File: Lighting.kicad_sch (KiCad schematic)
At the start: 5 parts, among them U4 TXS0101DBV

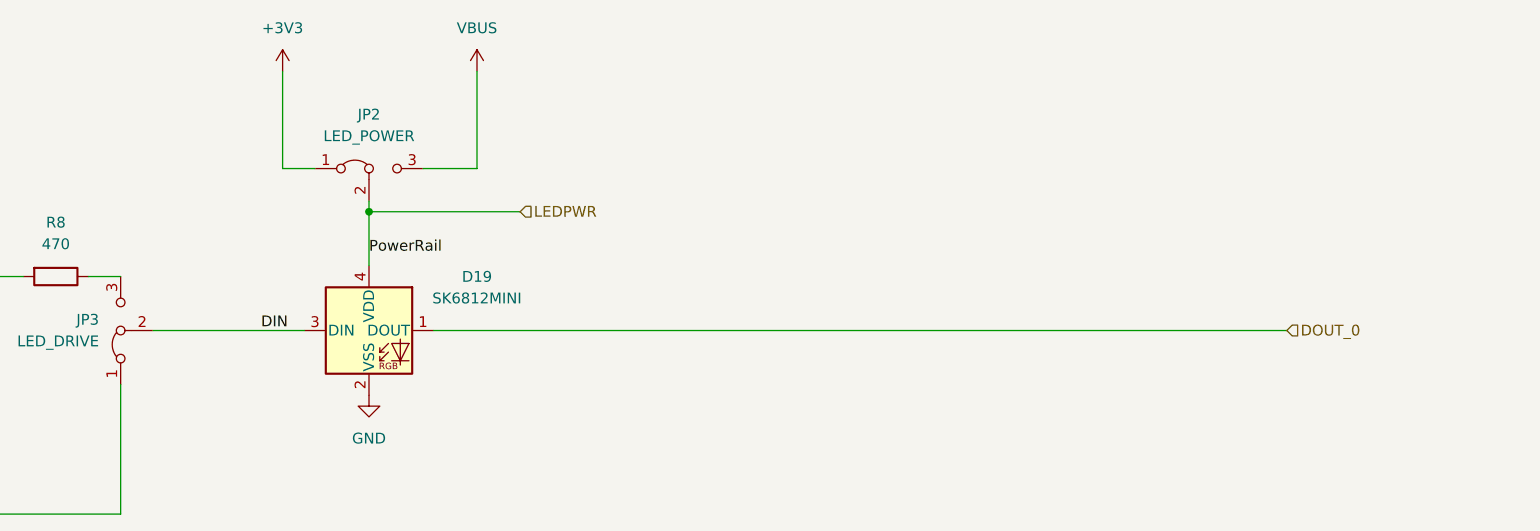
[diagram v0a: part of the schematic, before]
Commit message: WIP: Updated SK6812Mini to SK6812Mini-E and remapped ref des keys between PCB and Schematic.
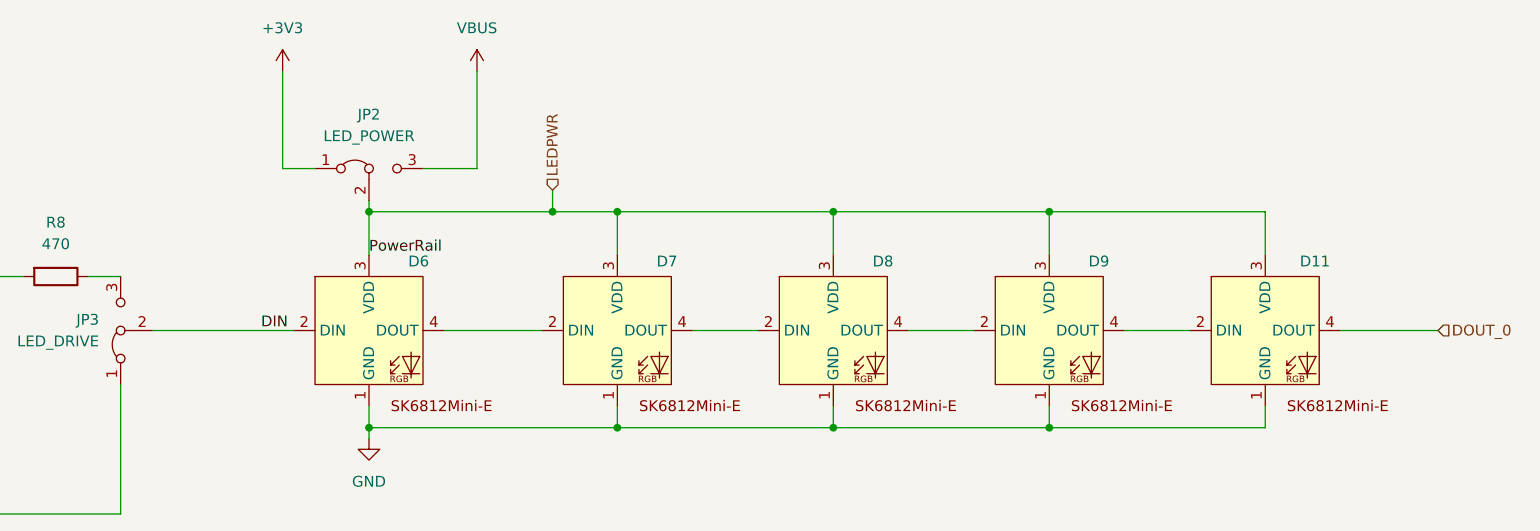
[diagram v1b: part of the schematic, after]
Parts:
- removed D19: SK6812MINI, LED_SMD:LED_SK6812MINI_PLCC4_3.5x3.5mm_P1.75mm, symbol LED:SK6812MINI
- added D11, D6, D7, D8, D9: ~, Extra:SK6812-MINI-E_ReverseMount, symbol Extra:SK6812Mini-E
- JP2, JP3: footprint (none) -> Connector_PinSocket_2.54mm:PinSocket_1x03_P2.54mm_Vertical
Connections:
- net DIN: now also D6.2 (DIN)
- net DOUT_0: now also D11.4 (DOUT)
- net GND: now also D11.1 (GND), D6.1 (GND), D7.1 (GND), D8.1 (GND), D9.1 (GND)
- net LEDPWR: now also D11.3 (VDD), D6.3 (VDD), D7.3 (VDD), D8.3 (VDD), D9.3 (VDD)
- new net: D8.4 (DOUT), D9.2 (DIN)
- new net: D11.2 (DIN), D9.4 (DOUT)
- new net: D6.4 (DOUT), D7.2 (DIN)
- new net: D7.4 (DOUT), D8.2 (DIN)

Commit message: Placing nearly all components onto the PCB. Removing the 9Vto5V battery input stage from populating onto the PCB.
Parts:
- R8: footprint Resistor_SMD:R_0603_1608Metric_Pad0.98x0.95mm_HandSolder -> Resistor_SMD:R_0805_2012Metric_Pad1.20x1.40mm_HandSolder
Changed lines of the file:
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@@
 			)
 		)
-		(property "Footprint" "Resistor_SMD:R_0603_1608Metric_Pad0.98x0.95mm_HandSolder"
+		(property "Footprint" "Resistor_SMD:R_0805_2012Metric_Pad1.20x1.40mm_HandSolder"
 			(at 88.9 47.752 90)
 			(effects

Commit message: Added testpoints, finished placing components, fixed footprint mapping, and ready to start routing tracks.
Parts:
- removed D11: ~, Extra:SK6812-MINI-E_ReverseMount, symbol Extra:SK6812Mini-E
- JP2, JP3: footprint Connector_PinSocket_2.54mm:PinSocket_1x03_P2.54mm_Vertical -> Connector_PinHeader_2.54mm:PinHeader_1x03_P2.54mm_Vertical
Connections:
- net DOUT_0: now also D9.4 (DOUT)
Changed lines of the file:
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@@
-	)
-	(junction
-		(at 205.74 67.31)
-		(diameter 0)
-		(color 0 0 0 0)
 	)
 	(junction
@@
 	)
 	(junction
-		(at 205.74 41.91)
-		(diameter 0)
-		(color 0 0 0 0)
-	)
-	(junction
 		(at 154.94 41.91)
 		(diameter 0)
@@
 	(wire
 		(pts
-			(xy 205.74 41.91) (xy 231.14 41.91)
-		)
-		(stroke
-			(width 0)
-			(type default)
-		)
-	)
-	(wire
-		(pts
 			(xy 132.08 36.83) (xy 138.43 36.83)
 		)
@@
 	(wire
 		(pts
-			(xy 240.03 55.88) (xy 251.46 55.88)
-		)
-		(stroke
-			(width 0)
-			(type default)
-		)
-	)
-	(wire
-		(pts
 			(xy 180.34 46.99) (xy 180.34 41.91)
 		)
@@
 	(wire
 		(pts
-			(xy 231.14 64.77) (xy 231.14 67.31)
-		)
-		(stroke
-			(width 0)
-			(type default)
-		)
-	)
-	(wire
-		(pts
 			(xy 205.74 46.99) (xy 205.74 41.91)
 		)
@@
 	(wire
 		(pts
-			(xy 231.14 46.99) (xy 231.14 41.91)
-		)
-		(stroke
-			(width 0)
-			(type default)
-		)
-	)
-	(wire
-		(pts
 			(xy 154.94 46.99) (xy 154.94 41.91)
 		)
@@
 		(pts
 			(xy 180.34 41.91) (xy 205.74 41.91)
-		)
-		(stroke
-			(width 0)
-			(type default)
-		)
-	)
-	(wire
-		(pts
-			(xy 205.74 67.31) (xy 231.14 67.31)
 		)
 		(stroke
@@
 	(hierarchical_label "DOUT_0"
 		(shape input)
-		(at 251.46 55.88 0)
+		(at 222.25 55.88 0)
 		(fields_autoplaced yes)
 		(effects
@@
 			)
 		)
-		(property "Footprint" "Connector_PinSocket_2.54mm:PinSocket_1x03_P2.54mm_Vertical"
+		(property "Footprint" "Connector_PinHeader_2.54mm:PinHeader_1x03_P2.54mm_Vertical"
 			(at 125.73 36.83 0)
 			(effects
@@
 	)
 	(symbol
-		(lib_id "Extra:SK6812Mini-E")
-		(at 231.14 55.88 0)
-		(unit 1)
-		(exclude_from_sim no)
-		(in_bom yes)
-		(on_board yes)
-		(dnp no)
-		(property "Reference" "D11"
-			(at 236.982 47.752 0)
-			(effects
-				(font
-					(size 1.27 1.27)
-				)
-			)
-		)
-		(property "Value" "~"
-			(at 250.19 52.7365 0)
-			(effects
-				(font
-					(size 1.27 1.27)
-				)
-			)
-		)
-		(property "Footprint" "Extra:SK6812-MINI-E_ReverseMount"
-			(at 231.14 55.88 0)
-			(effects
-				(font
-					(size 1.27 1.27)
-				)
-				(hide yes)
-			)
-		)
-		(property "Datasheet" ""
-			(at 231.14 55.88 0)
-			(effects
-				(font
-					(size 1.27 1.27)
-				)
-				(hide yes)
-			)
-		)
-		(property "Description" ""
-			(at 231.14 55.88 0)
-			(effects
-				(font
-					(size 1.27 1.27)
-				)
-				(hide yes)
-			)
-		)
-		(pin "3"
-		)
-		(pin "4"
-		)
-		(pin "1"
-		)
-		(pin "2"
-		)
-		(instances
-			(project "WeddingCenterPieces"
-				(path "/4e0ee48d-0121-4621-a533-4795bdfb88f1/959cab23-3f14-4c5e-8fa4-11c71d6f64e0"
-					(reference "D11")
-					(unit 1)
-				)
-			)
-		)
-	)
-	(symbol
 		(lib_id "power:VBUS")
 		(at 138.43 25.4 0)
@@
 			)
 		)
-		(property "Footprint" "Connector_PinSocket_2.54mm:PinSocket_1x03_P2.54mm_Vertical"
+		(property "Footprint" "Connector_PinHeader_2.54mm:PinHeader_1x03_P2.54mm_Vertical"
 			(at 96.52 55.88 0)
 			(effects

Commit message: Updating SK6812 circuit to match suggested application from datasheet, adding a resistor at the last DOut and filter caps to each LED.
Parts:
- added C19, C2, C20, C21: 100nF, Capacitor_SMD:C_0805_2012Metric_Pad1.18x1.45mm_HandSolder, symbol Device:C
- added R15: 470, Resistor_SMD:R_0805_2012Metric_Pad1.20x1.40mm_HandSolder, symbol Device:R
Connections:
- net DIN: now also R8.1; no longer JP3.2 (C)
- net DOUT_0: now also R15.1; no longer D9.4 (DOUT)
- net GND: now also C19.2, C2.2, C20.2, C21.2
- net LEDPWR: now also C19.1, C2.1, C20.1, C21.1
- net at JP3.3 (B): now also U4.4 (B); no longer R8.1
- net at R8.2: now also JP3.2 (C); no longer U4.4 (B)
- new net: D9.4 (DOUT), R15.2
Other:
- moved on the sheet: JP3, R8

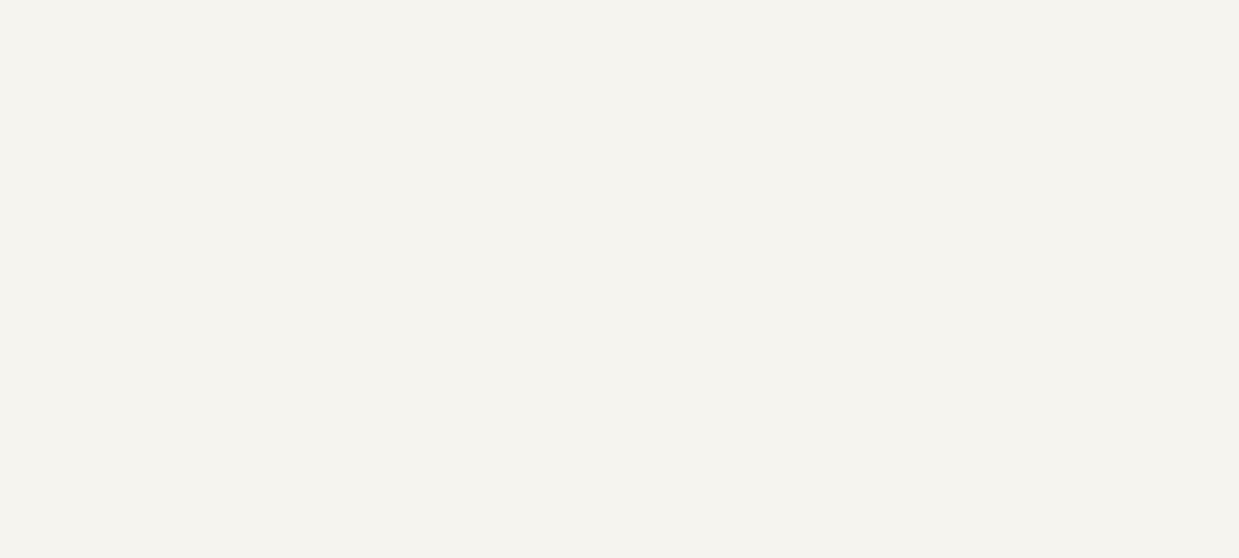
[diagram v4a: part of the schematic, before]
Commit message: Adding additional LEDs and driver to test per-key LEDs, updating net classes and design constraints, and starting to route tracks.
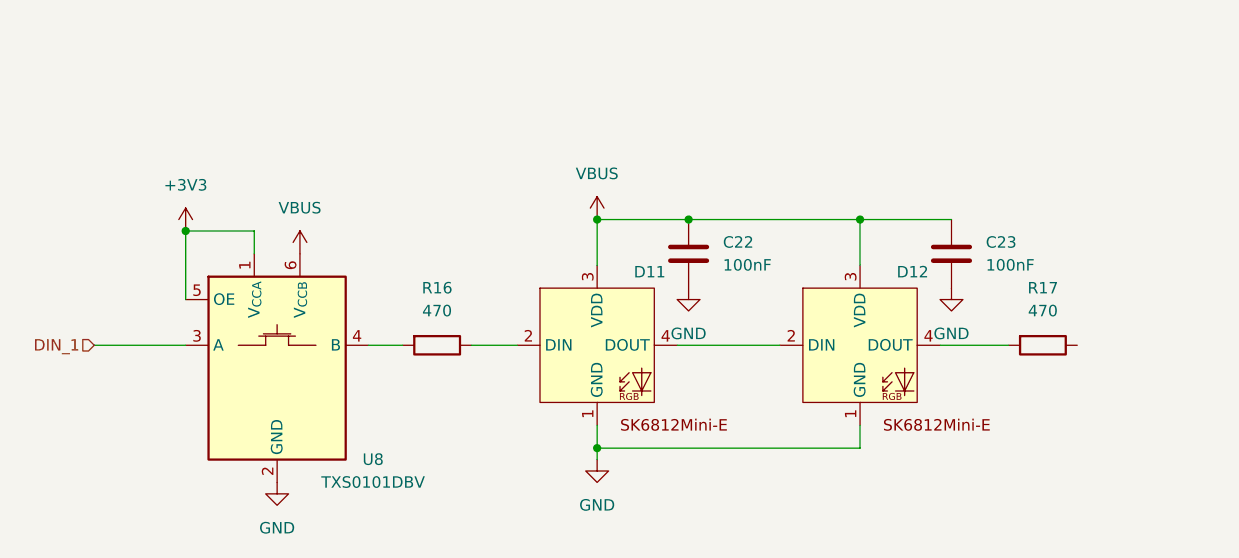
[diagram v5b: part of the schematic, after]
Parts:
- added C22, C23: 100nF, Capacitor_SMD:C_0805_2012Metric_Pad1.18x1.45mm_HandSolder, symbol Device:C
- added D11, D12: ~, Extra:SK6812-MINI-E_ReverseMount, symbol Extra:SK6812Mini-E
- added R16, R17: 470, Resistor_SMD:R_0805_2012Metric_Pad1.20x1.40mm_HandSolder, symbol Device:R
- added U8: TXS0101DBV, Package_TO_SOT_SMD:SOT-23-6, symbol Logic_LevelTranslator:TXS0101DBV
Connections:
- net +3V3: now also U8.1 (V_{CCA}), U8.5 (OE)
- net GND: now also C22.2, C23.2, D11.1 (GND), D12.1 (GND), U8.2 (GND)
- net VBUS: now also C22.1, C23.1, D11.3 (VDD), D12.3 (VDD), U8.6 (V_{CCB})
- new net: D11.4 (DOUT), D12.2 (DIN)
- new net: D12.4 (DOUT), R17.2
- new net: D11.2 (DIN), R16.1
- new net: R16.2, U8.4 (B)
- new net DIN_1: U8.3 (A)

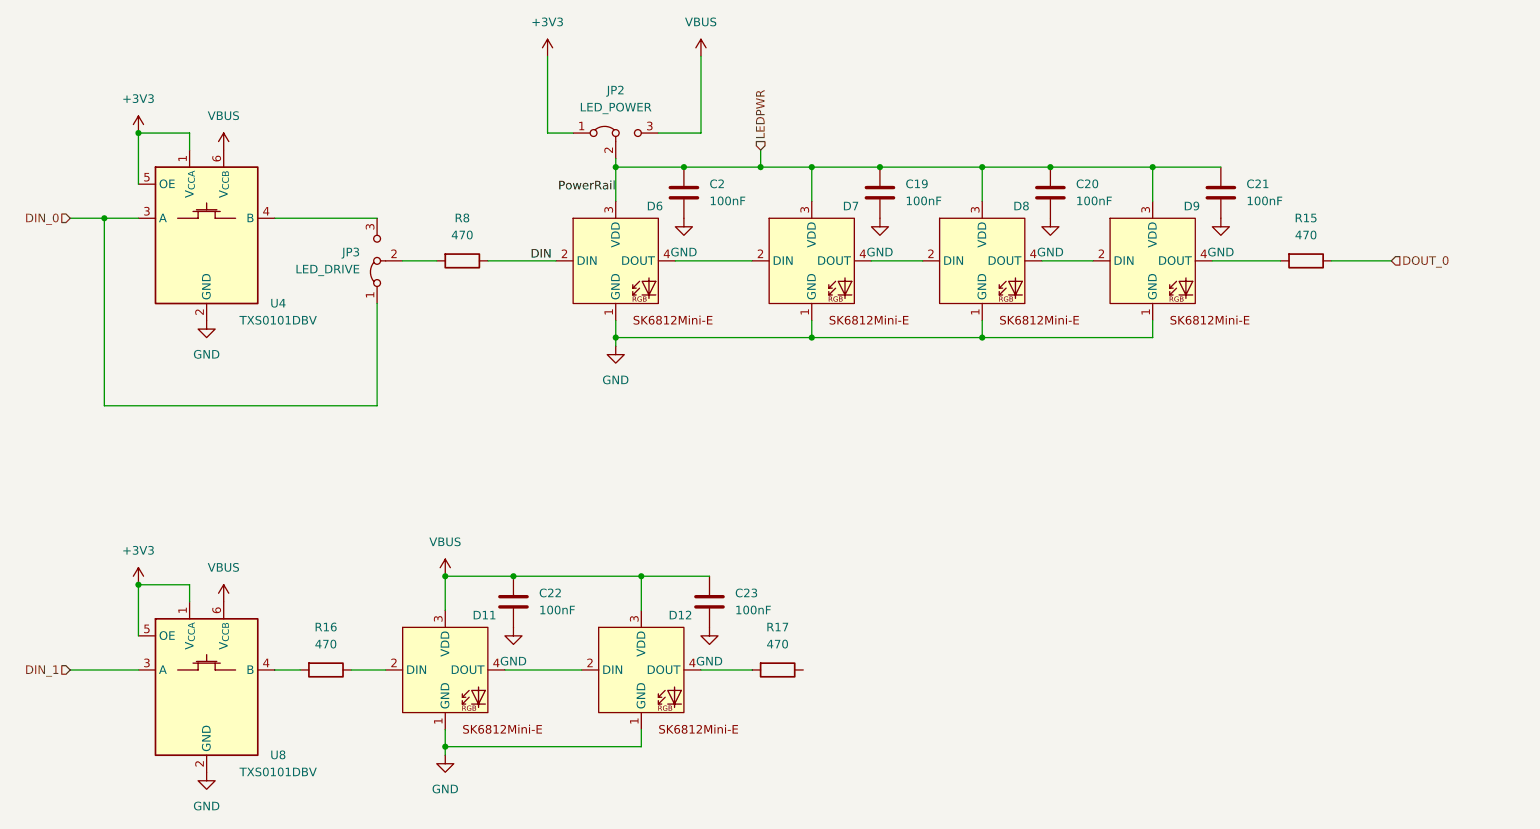
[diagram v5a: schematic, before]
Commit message: Shrinking board to only have 2 key switches and a few other unnecessary components. Finished with routing the rest of the board.
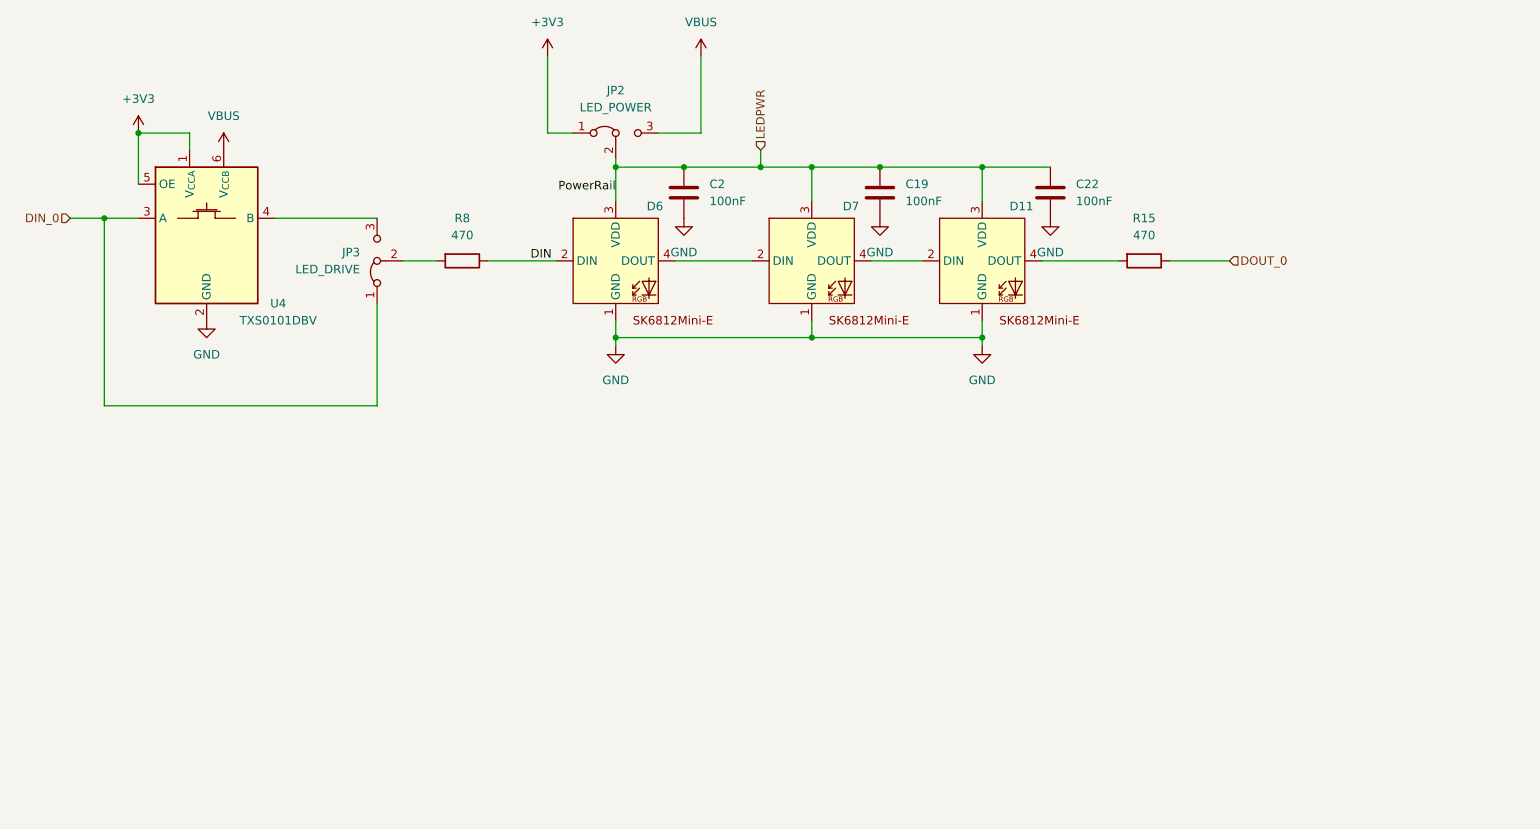
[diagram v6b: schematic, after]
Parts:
- removed C20, C21, C23: 100nF, Capacitor_SMD:C_0805_2012Metric_Pad1.18x1.45mm_HandSolder, symbol Device:C
- removed D12, D8, D9: ~, Extra:SK6812-MINI-E_ReverseMount, symbol Extra:SK6812Mini-E
- removed R16, R17: 470, Resistor_SMD:R_0805_2012Metric_Pad1.20x1.40mm_HandSolder, symbol Device:R
- removed U8: TXS0101DBV, Package_TO_SOT_SMD:SOT-23-6, symbol Logic_LevelTranslator:TXS0101DBV
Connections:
- net LEDPWR: now also C22.1, D11.3 (VDD)
- net VBUS: no longer C22.1, D11.3 (VDD)
- net at D11.4 (DOUT): now also R15.2
- net at D11.2 (DIN): now also D7.4 (DOUT)
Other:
- moved on the sheet: C22, D11, R15
